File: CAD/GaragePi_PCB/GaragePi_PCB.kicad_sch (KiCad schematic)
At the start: 13 parts, among them J1 Screw_Terminal_01x03, J2 Screw_Terminal_01x03, J3 Raspberry_Pi_2_3, J4 Screw_Terminal_01x03, J5 Screw_Terminal_01x03, K1 SANYOU_SRD_Form_C, K2 SANYOU_SRD_Form_C, Q1 PN2222A, Q2 PN2222A

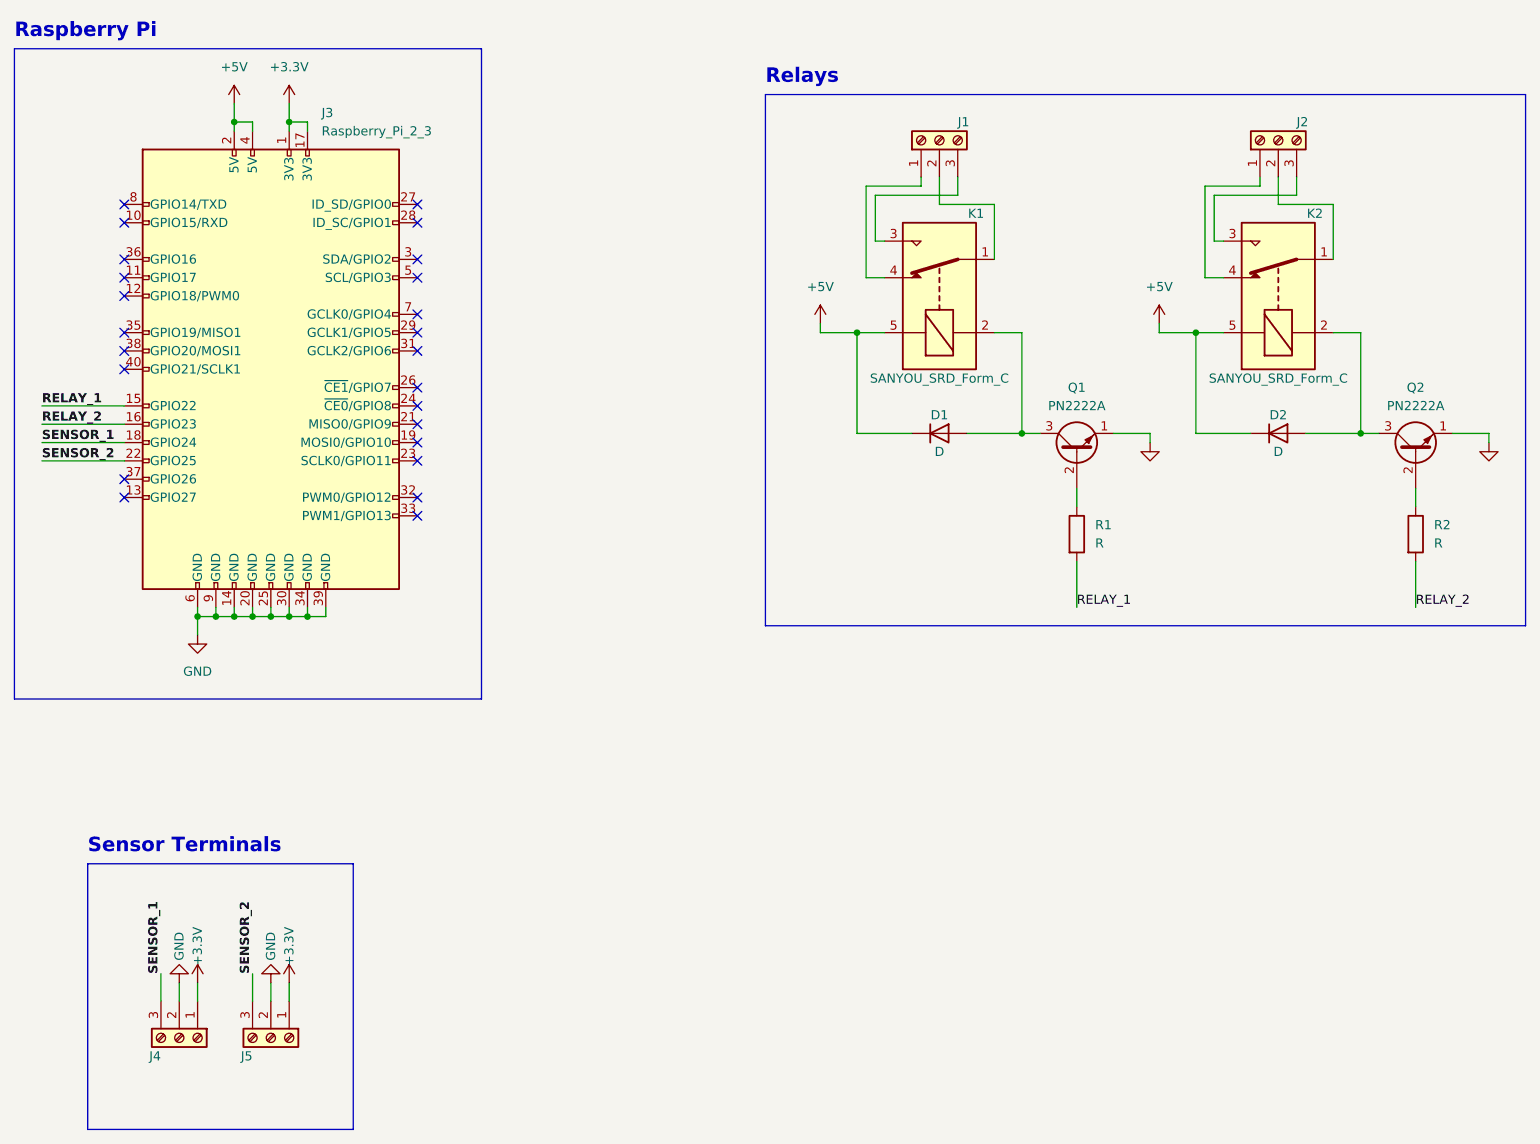
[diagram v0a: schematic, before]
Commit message: completed PCB schematics v0.1; Updated README with the project update
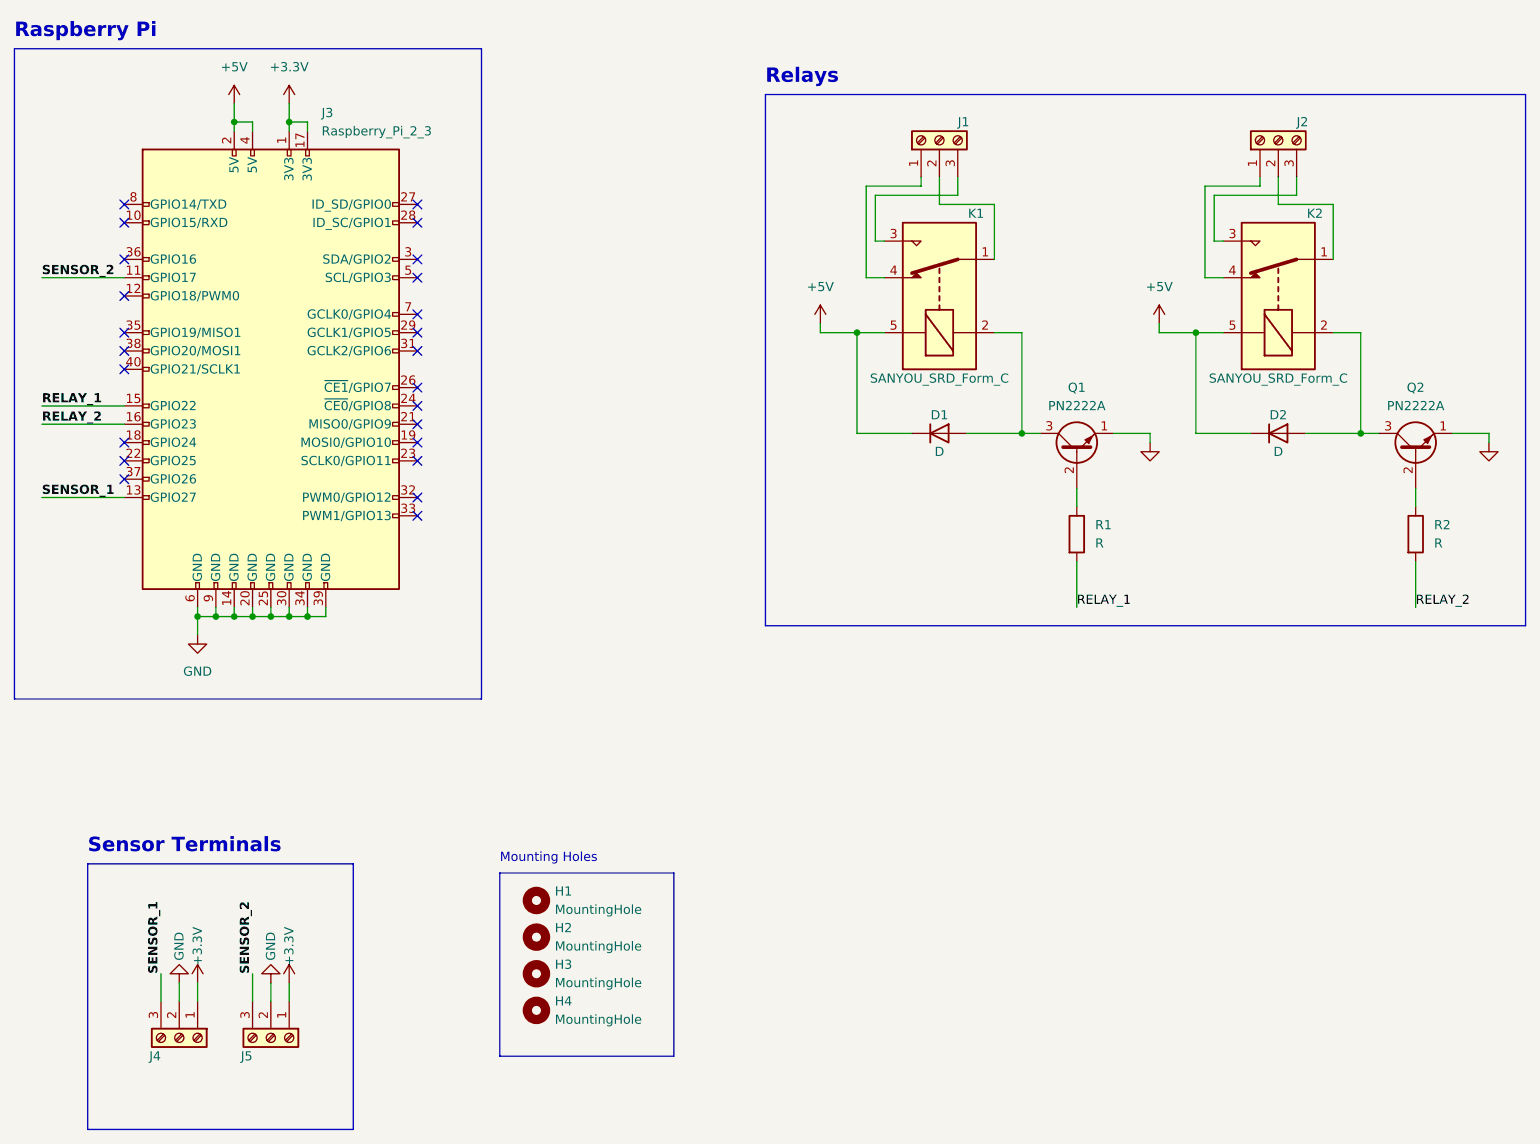
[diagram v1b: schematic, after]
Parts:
- added H1, H2, H3, H4: MountingHole, MountingHole:MountingHole_2.7mm_M2.5, symbol Mechanical:MountingHole
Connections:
- net SENSOR_1: now also J3.13 (GPIO27); no longer J3.18 (GPIO24)
- net SENSOR_2: now also J3.11 (GPIO17); no longer J3.22 (GPIO25)
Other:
- note added: "Mounting Holes"
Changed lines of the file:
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@@
   (no_connect (at 102.87 74.93))
   (no_connect (at 102.87 69.85))
-  (no_connect (at 62.23 54.61))
   (no_connect (at 62.23 64.77))
   (no_connect (at 62.23 62.23))
@@
   (no_connect (at 102.87 85.09))
   (no_connect (at 102.87 54.61))
-  (no_connect (at 62.23 85.09))
   (no_connect (at 62.23 82.55))
   (no_connect (at 62.23 57.15))
@@
   (no_connect (at 102.87 64.77))
   (no_connect (at 102.87 46.99))
+  (no_connect (at 62.23 80.01))
   (no_connect (at 102.87 87.63))
   (no_connect (at 62.23 67.31))
   (no_connect (at 102.87 62.23))
+  (no_connect (at 62.23 77.47))
   (wire (pts (xy 50.8 74.93) (xy 62.23 74.93))
     (stroke (width 0) (type default))
@@
     (stroke (width 0) (type default))
   )
+  (polyline (pts (xy 114.3 137.16) (xy 114.3 162.56))
+    (stroke (width 0) (type default))
+  )
   (wire (pts (xy 251.46 76.2) (xy 251.46 77.47))
     (stroke (width 0) (type default))
@@
     (stroke (width 0) (type default))
   )
+  (polyline (pts (xy 114.3 137.16) (xy 138.43 137.16))
+    (stroke (width 0) (type default))
+  )
   (wire (pts (xy 233.68 76.2) (xy 236.22 76.2))
     (stroke (width 0) (type default))
@@
     (stroke (width 0) (type default))
   )
-  (wire (pts (xy 50.8 80.01) (xy 62.23 80.01))
+  (wire (pts (xy 50.8 85.09) (xy 62.23 85.09))
     (stroke (width 0) (type default))
   )
@@
     (stroke (width 0) (type default))
   )
-  (wire (pts (xy 50.8 77.47) (xy 62.23 77.47))
+  (wire (pts (xy 50.8 54.61) (xy 62.23 54.61))
     (stroke (width 0) (type default))
   )
@@
     (stroke (width 0) (type default))
   )
+  (polyline (pts (xy 138.43 162.56) (xy 138.43 137.16))
+    (stroke (width 0) (type default))
+  )
   (wire (pts (xy 172.72 41.91) (xy 172.72 40.64))
     (stroke (width 0) (type default))
   )
+  (polyline (pts (xy 114.3 162.56) (xy 138.43 162.56))
+    (stroke (width 0) (type default))
+  )
   (wire (pts (xy 80.01 33.02) (xy 80.01 34.29))
     (stroke (width 0) (type default))
@@
   (polyline (pts (xy 256.54 102.87) (xy 256.54 29.21))
     (stroke (width 0) (type default))
+  )
+  (text "Mounting Holes" (at 114.3 135.89 0)
+    (effects (font (size 1.27 1.27)) (justify left bottom))
   )
   (text "Sensor Terminals" (at 57.15 134.62 0)
@@
     (effects (font (size 1.27 1.27) bold) (justify left bottom))
   )
-  (label "SENSOR_1" (at 50.8 77.47 0) (fields_autoplaced)
+  (label "SENSOR_1" (at 50.8 85.09 0) (fields_autoplaced)
     (effects (font (size 1.27 1.27) bold) (justify left bottom))
   )
-  (label "SENSOR_2" (at 50.8 80.01 0) (fields_autoplaced)
+  (label "SENSOR_2" (at 50.8 54.61 0) (fields_autoplaced)
     (effects (font (size 1.27 1.27) bold) (justify left bottom))
   )
@@
         (path "/9c4866a2-af57-4723-87a8-479afaded34f"
           (reference "Q1") (unit 1)
+        )
+      )
+    )
+  )
+  (symbol (lib_id "Mechanical:MountingHole") (at 119.38 151.13 0) (unit 1)
+    (in_bom yes) (on_board yes) (dnp no) (fields_autoplaced)
+    (property "Reference" "H3" (at 121.92 149.86 0)
+      (effects (font (size 1.27 1.27)) (justify left))
+    )
+    (property "Value" "MountingHole" (at 121.92 152.4 0)
+      (effects (font (size 1.27 1.27)) (justify left))
+    )
+    (property "Footprint" "MountingHole:MountingHole_2.7mm_M2.5" (at 119.38 151.13 0)
+      (effects (font (size 1.27 1.27)) hide)
+    )
+    (property "Datasheet" "~" (at 119.38 151.13 0)
+      (effects (font (size 1.27 1.27)) hide)
+    )
+    (instances
+      (project "GaragePi_PCB"
+        (path "/9c4866a2-af57-4723-87a8-479afaded34f"
+          (reference "H3") (unit 1)
         )
       )
@@
     )
   )
+  (symbol (lib_id "Mechanical:MountingHole") (at 119.38 146.05 0) (unit 1)
+    (in_bom yes) (on_board yes) (dnp no) (fields_autoplaced)
+    (property "Reference" "H2" (at 121.92 144.78 0)
+      (effects (font (size 1.27 1.27)) (justify left))
+    )
+    (property "Value" "MountingHole" (at 121.92 147.32 0)
+      (effects (font (size 1.27 1.27)) (justify left))
+    )
+    (property "Footprint" "MountingHole:MountingHole_2.7mm_M2.5" (at 119.38 146.05 0)
+      (effects (font (size 1.27 1.27)) hide)
+    )
+    (property "Datasheet" "~" (at 119.38 146.05 0)
+      (effects (font (size 1.27 1.27)) hide)
+    )
+    (instances
+      (project "GaragePi_PCB"
+        (path "/9c4866a2-af57-4723-87a8-479afaded34f"
+          (reference "H2") (unit 1)
+        )
+      )
+    )
+  )
   (symbol (lib_id "power:+5V") (at 158.75 60.96 0) (unit 1)
     (in_bom yes) (on_board yes) (dnp no) (fields_autoplaced)
@@
         )
       )
+    )
+  )
+  (symbol (lib_id "Mechanical:MountingHole") (at 119.38 156.21 0) (unit 1)
+    (in_bom yes) (on_board yes) (dnp no) (fields_autoplaced)
+    (property "Reference" "H4" (at 121.92 154.94 0)
+      (effects (font (size 1.27 1.27)) (justify left))
+    )
+    (property "Value" "MountingHole" (at 121.92 157.48 0)
+      (effects (font (size 1.27 1.27)) (justify left))
+    )
+    (property "Footprint" "MountingHole:MountingHole_2.7mm_M2.5" (at 119.38 156.21 0)
+      (effects (font (size 1.27 1.27)) hide)
+    )
+    (property "Datasheet" "~" (at 119.38 156.21 0)
+      (effects (font (size 1.27 1.27)) hide)
+    )
+    (instances
+      (project "GaragePi_PCB"
+        (path "/9c4866a2-af57-4723-87a8-479afaded34f"
+          (reference "H4") (unit 1)
+        )
+      )
+    )
+  )
+  (symbol (lib_id "Mechanical:MountingHole") (at 119.38 140.97 0) (unit 1)
+    (in_bom yes) (on_board yes) (dnp no) (fields_autoplaced)
+    (property "Reference" "H1" (at 121.92 139.7 0)
+      (effects (font (size 1.27 1.27)) (justify left))
+    )
+    (property "Value" "MountingHole" (at 121.92 142.24 0)
+      (effects (font (size 1.27 1.27)) (justify left))
+    )
+    (property "Footprint" "MountingHole:MountingHole_2.7mm_M2.5" (at 119.38 140.97 0)
+      (effects (font (size 1.27 1.27)) hide)
+    )
+    (property "Datasheet" "~" (at 119.38 140.97 0)
+      (effects (font (size 1.27 1.27)) hide)
+    )
+    (instances
+      (project "GaragePi_PCB"
+        (path "/9c4866a2-af57-4723-87a8-479afaded34f"
+          (reference "H1") (unit 1)
+        )
+      )
